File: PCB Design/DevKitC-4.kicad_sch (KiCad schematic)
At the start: 18 parts, among them J1 Screw_Terminal_01x02, J2 Screw_Terminal_01x02, J3 Screw_Terminal_01x04, J5 Screw_Terminal_01x03, Q1 IRLZ44N, SW1 SW_DPDT_x2, U1 ESP32-DevKitC, U2 Generic_5v_Module

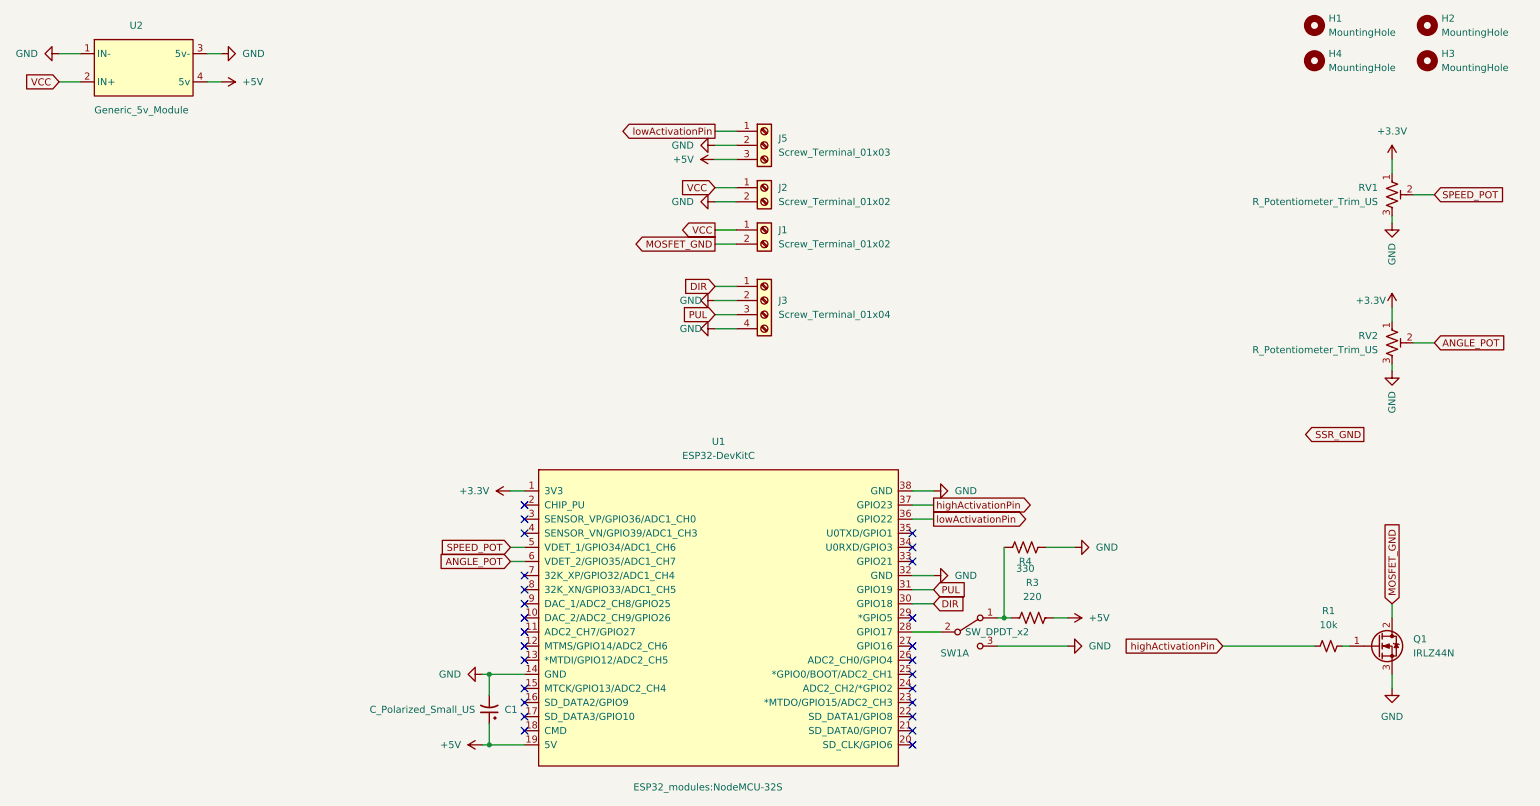
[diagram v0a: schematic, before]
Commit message: Squashed commit of the following:
commit 8d3ad245b0b0885bf609d6c80dccf06c404355da
Author: Scott Dial <smdial@alumni.purdue.edu>
Date:   Sun Mar 26 20:17:48 2023 -0400

    updated pcb and arduino

commit aee9d78b6388df0d7588c47fb258c3b1a8245808
Author: Bullseye <90105099+100-5x@users.noreply.github.com>
Date:   Tue Feb 14 13:17:23 2023 -0500

    code changes.

    switched HIGH & LOW for the switch

commit 5ec61c4ec09789be3bb0214a7fa9b8cab35d8441
Author: Bullseye <90105099+100-5x@users.noreply.github.com>
Date:   Wed Feb 8 12:47:40 2023 -0500

    PCB Text Updates

commit 8f82cd768d246ead5170c5acd62d163460c6e75b
Author: Bullseye <90105099+100-5x@users.noreply.github.com>
Date:   Mon Feb 6 09:26:47 2023 -0500

    PCB & Code changes for version 2

    Added Diode to PCB
    Added Switch for Worker / Standalone
    Instructions on back silkscreen

commit 88eaa1f8307400ed63f43e3c574ed5baf0296be2
Author: Bullseye <90105099+100-5x@users.noreply.github.com>
Date:   Sun Jan 29 22:14:40 2023 -0500

    PCB and code changes for Dual Mode

commit 5d082f1582dbe39b2b10d9fe13ea9803484a0bf6
Author: Bullseye <90105099+100-5x@users.noreply.github.com>
Date:   Wed Jan 25 21:50:28 2023 -0600

    New file for dual work.
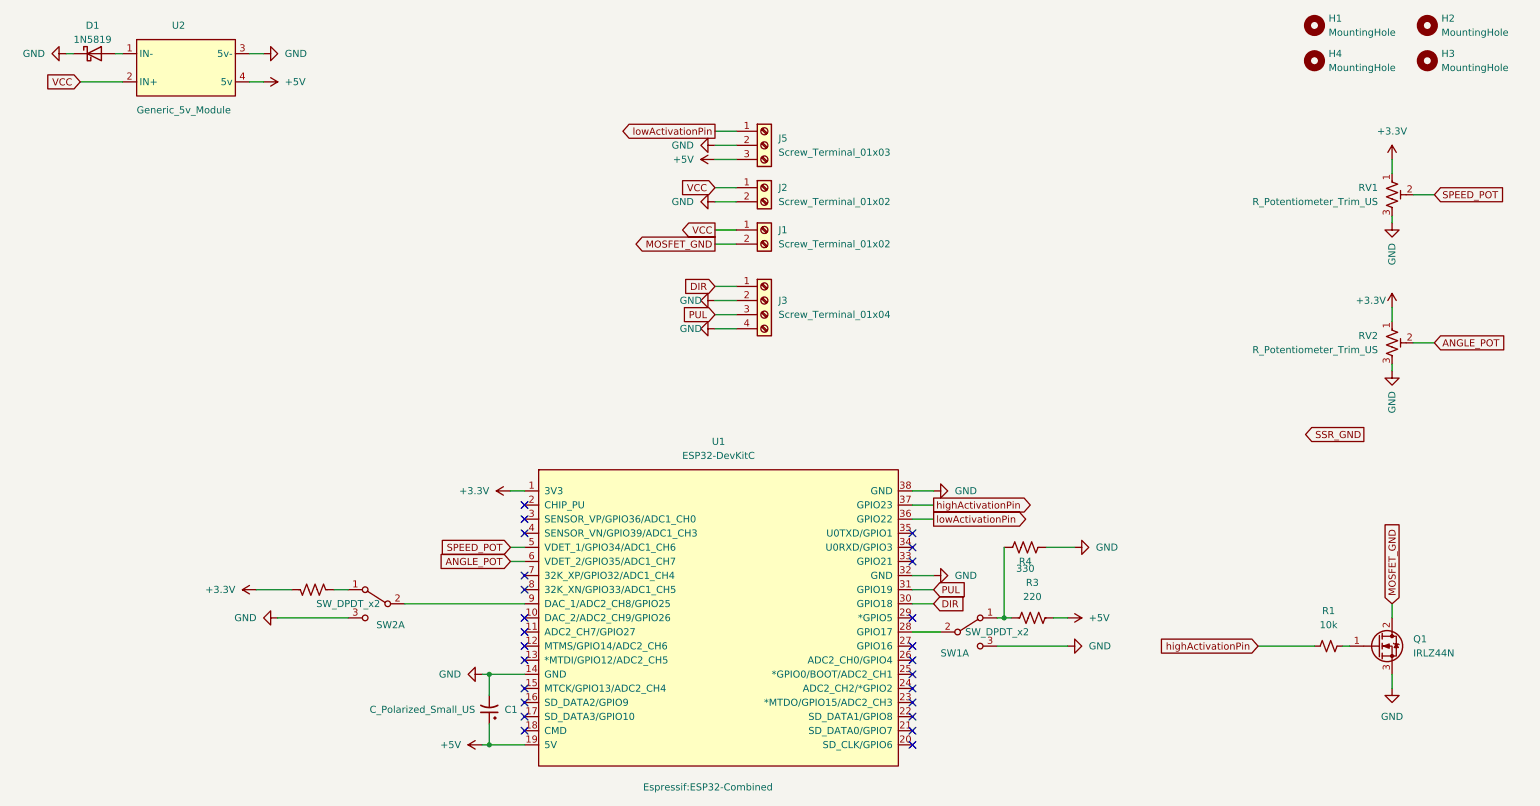
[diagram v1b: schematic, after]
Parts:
- added D1: 1N5819, Diode_THT:D_DO-41_SOD81_P10.16mm_Horizontal, symbol Diode:1N5819
- added R6: 220, Resistor_THT:R_Axial_DIN0207_L6.3mm_D2.5mm_P10.16mm_Horizontal, symbol Device:R_US
- added SW2: SW_DPDT_x2, Connector_PinHeader_2.54mm:PinHeader_1x03_P2.54mm_Vertical, symbol Switch:SW_DPDT_x2
- U1: footprint ESP32_modules:NodeMCU-32S -> Espressif:ESP32-Combined
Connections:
- net +3V3: now also R6.1
- net GND: now also D1.1 (K), SW2.3 (C); no longer U2.1 (IN-)
- net at U1.9 (DAC_1/ADC2_CH8/GPIO25): now also SW2.2 (B)
- new net: D1.2 (A), U2.1 (IN-)
- new net: R6.2, SW2.1 (A)
- no-connect marks 26 -> 25
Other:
- moved on the sheet: U2
